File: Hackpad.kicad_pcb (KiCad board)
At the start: 2 copper layers, 99 x 70 mm, 14 parts, among them SW1 SW_Push, SW2 SW_Push, SW3 SW_Push, SW4 SW_Push, SW5 SW_Push, SW6 RotaryEncoder_Switch_MP, U1 XIAO-RP2040-DIP

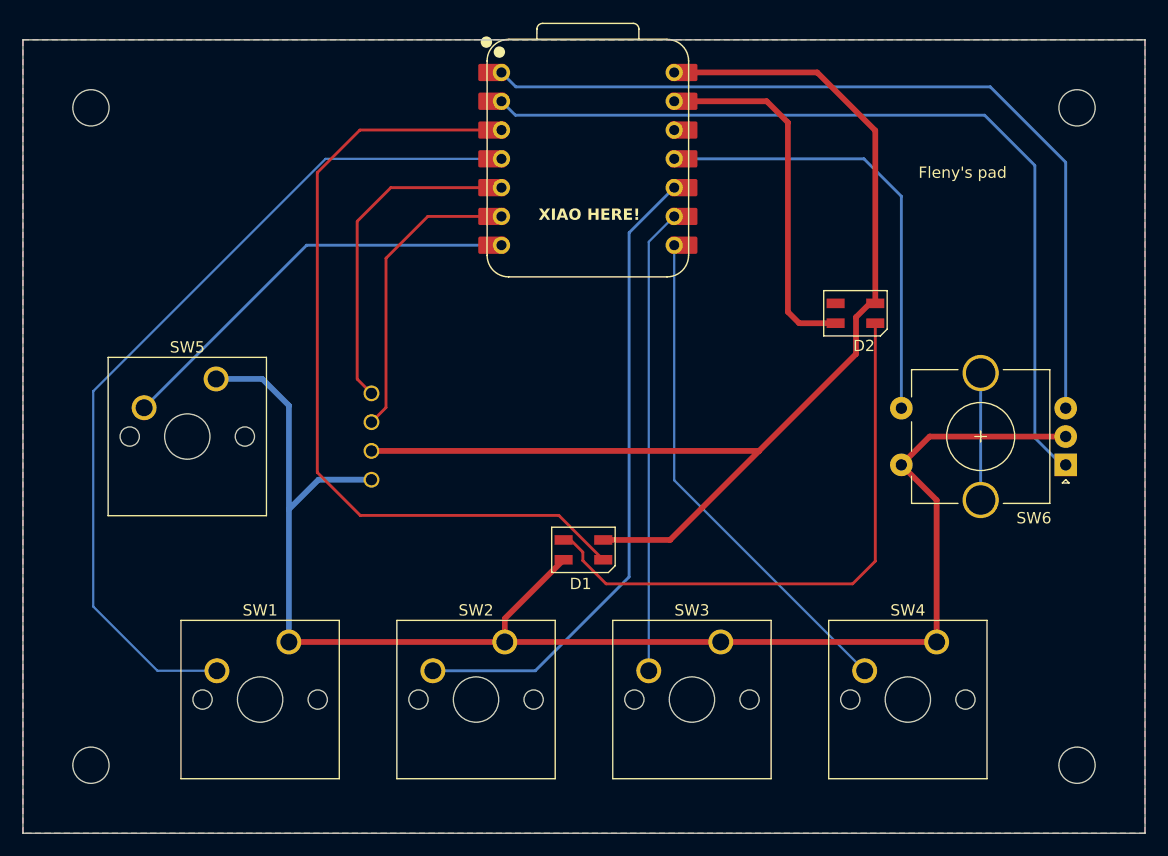
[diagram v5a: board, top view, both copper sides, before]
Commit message: 3D models & replace MX switch footprint
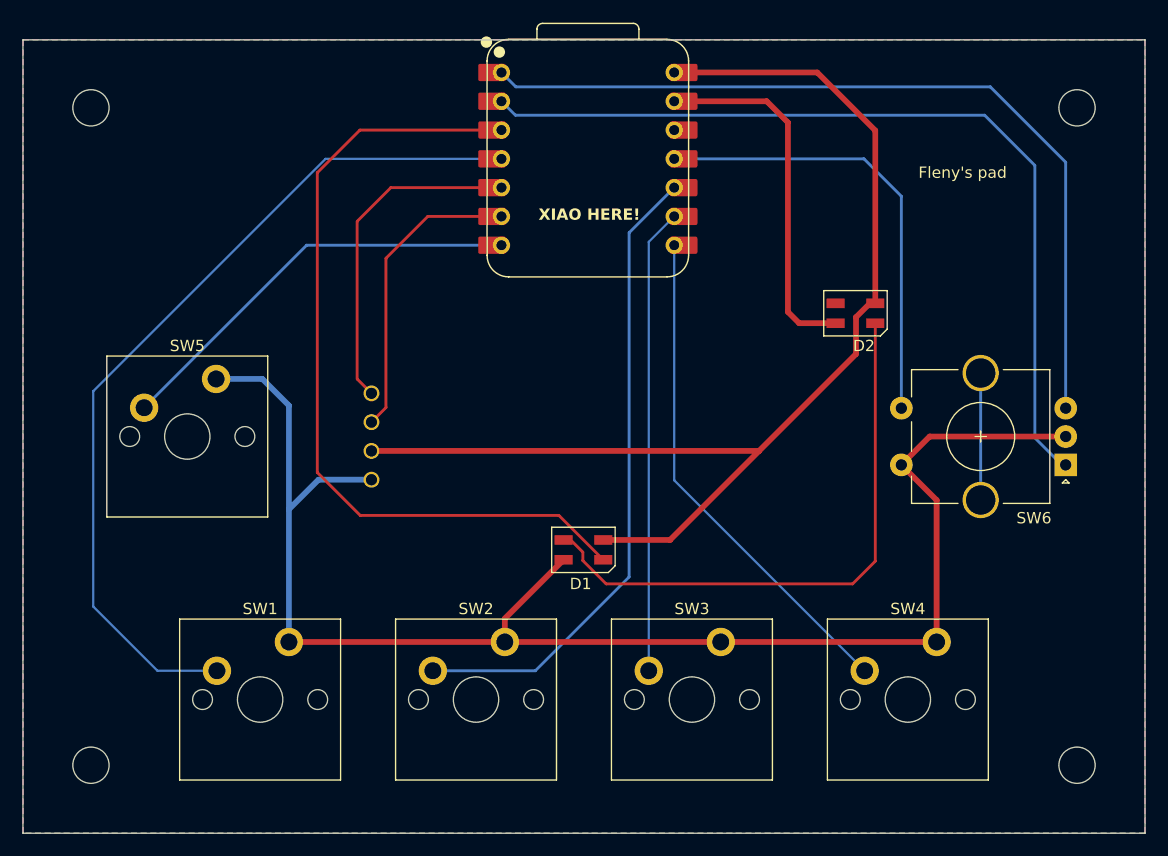
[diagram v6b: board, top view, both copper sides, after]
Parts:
- SW1, SW2, SW3, SW4, SW5: footprint Button_Switch_Keyboard:SW_Cherry_MX_1.00u_PCB -> Cherry MX:SW_Cherry_MX_PCB_1.00u
- moved SW4 5.68 mm to (143.1, 126.2)
- moved SW1 5.68 mm to (85.9, 126.2)
- moved SW2 5.68 mm to (105.0, 126.2)
- moved SW5 5.68 mm to (79.5, 103.0)
- moved SW3 5.68 mm to (124.0, 126.2)
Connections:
- SW1 pad 1: GND -> Net-(U1-GPIO29/ADC3/A3)
- SW1 pad 2: Net-(U1-GPIO29/ADC3/A3) -> GND
- SW2 pad 1: GND -> Net-(U1-GPIO4/MISO)
- SW2 pad 2: Net-(U1-GPIO4/MISO) -> GND
- SW3 pad 1: GND -> Net-(U1-GPIO2/SCK)
- SW3 pad 2: Net-(U1-GPIO2/SCK) -> GND
- SW4 pad 1: GND -> Net-(U1-GPIO1/RX)
- SW4 pad 2: Net-(U1-GPIO1/RX) -> GND
- SW5 pad 1: GND -> Net-(U1-GPIO0/TX)
- SW5 pad 2: Net-(U1-GPIO0/TX) -> GND
